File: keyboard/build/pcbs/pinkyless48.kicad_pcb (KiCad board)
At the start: 2 copper layers, 141.4 x 137.9 mm, 51 parts

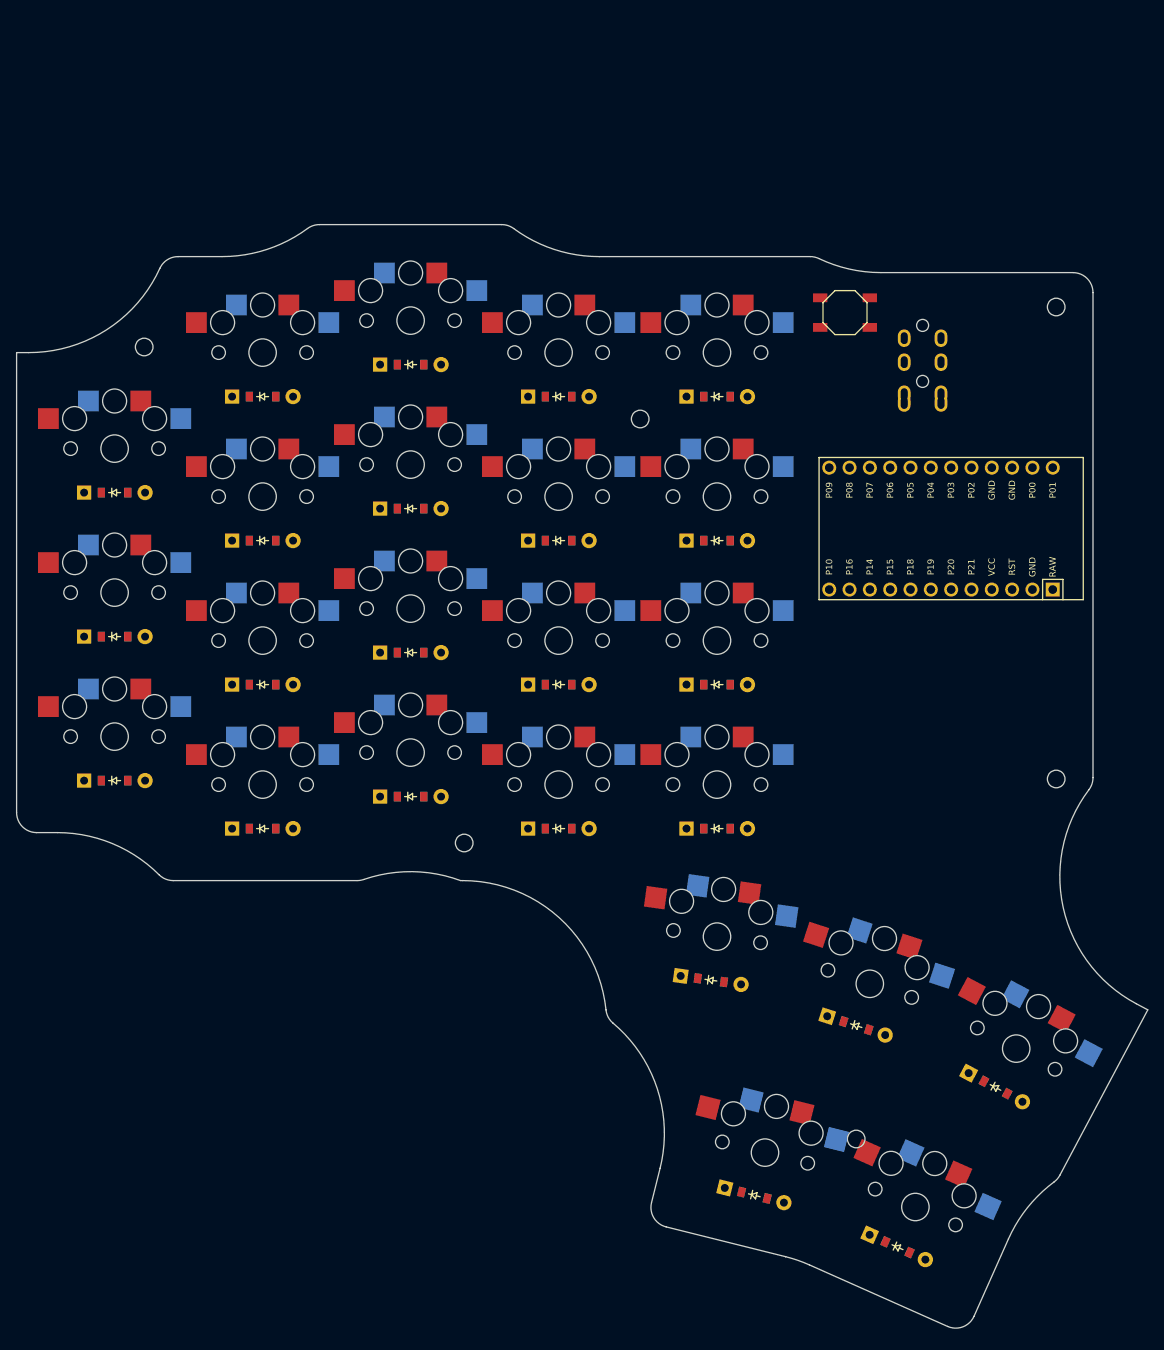
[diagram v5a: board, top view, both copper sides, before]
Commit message: Rebuild the board silhouette from three simple shapes
The outline was the union of one grown rectangle per key, so every column
step and every rotated thumb key left its own scallop and fillet. Straight
runs were constantly interrupted by small arcs, which is exactly what makes a
case hard to build against.

It is now three primitives:

  1. the finger matrix as ONE rectangle spanning every column and row,
     sized parametrically from kx/ky/kx_inner and the staggers
  2. the thumb cluster as a hull over its five keys, with `extend` so the
     hull wraps the key pads rather than the key centres
  3. the controller area as a rectangle

Measured: the fabricated outline goes from a scalloped perimeter to 9 straight
lines + 12 arcs + 6 screw holes, for about 1 cm^2 more copper and a slightly
smaller bounding box (136.4 x 134.1 mm, was 141.4 x 137.9).

This also makes two earlier workarounds redundant, both now removed: the `web`
patch zone that plugged a gap between unioned thumb pads, and the bridges
before it. A single rectangle cannot be disconnected from itself and a hull is
convex, so there is nothing left to bridge.

Fixed a mirroring bug found while rebuilding the preview's right half: an
anchor `shift` on a mirror_ ref has its x auto-negated by ergogen, so the
right half needs the SAME expression as the left, not its negation. Negating
it manually double-flipped the matrix rectangle and put it 75 mm off. Note
that this is the opposite of `adjust` shifts, which are NOT mirrored - the two
behave differently and are easy to get backwards. Both are now commented.

All five checks pass. Case STLs, QMK keyboard.json and previews regenerated.

Co-Authored-By: Claude Opus 5 <noreply@anthropic.com>
Claude-Session: https://claude.ai/code/session_01TKXtddA7pBLooPYbDwxvxo
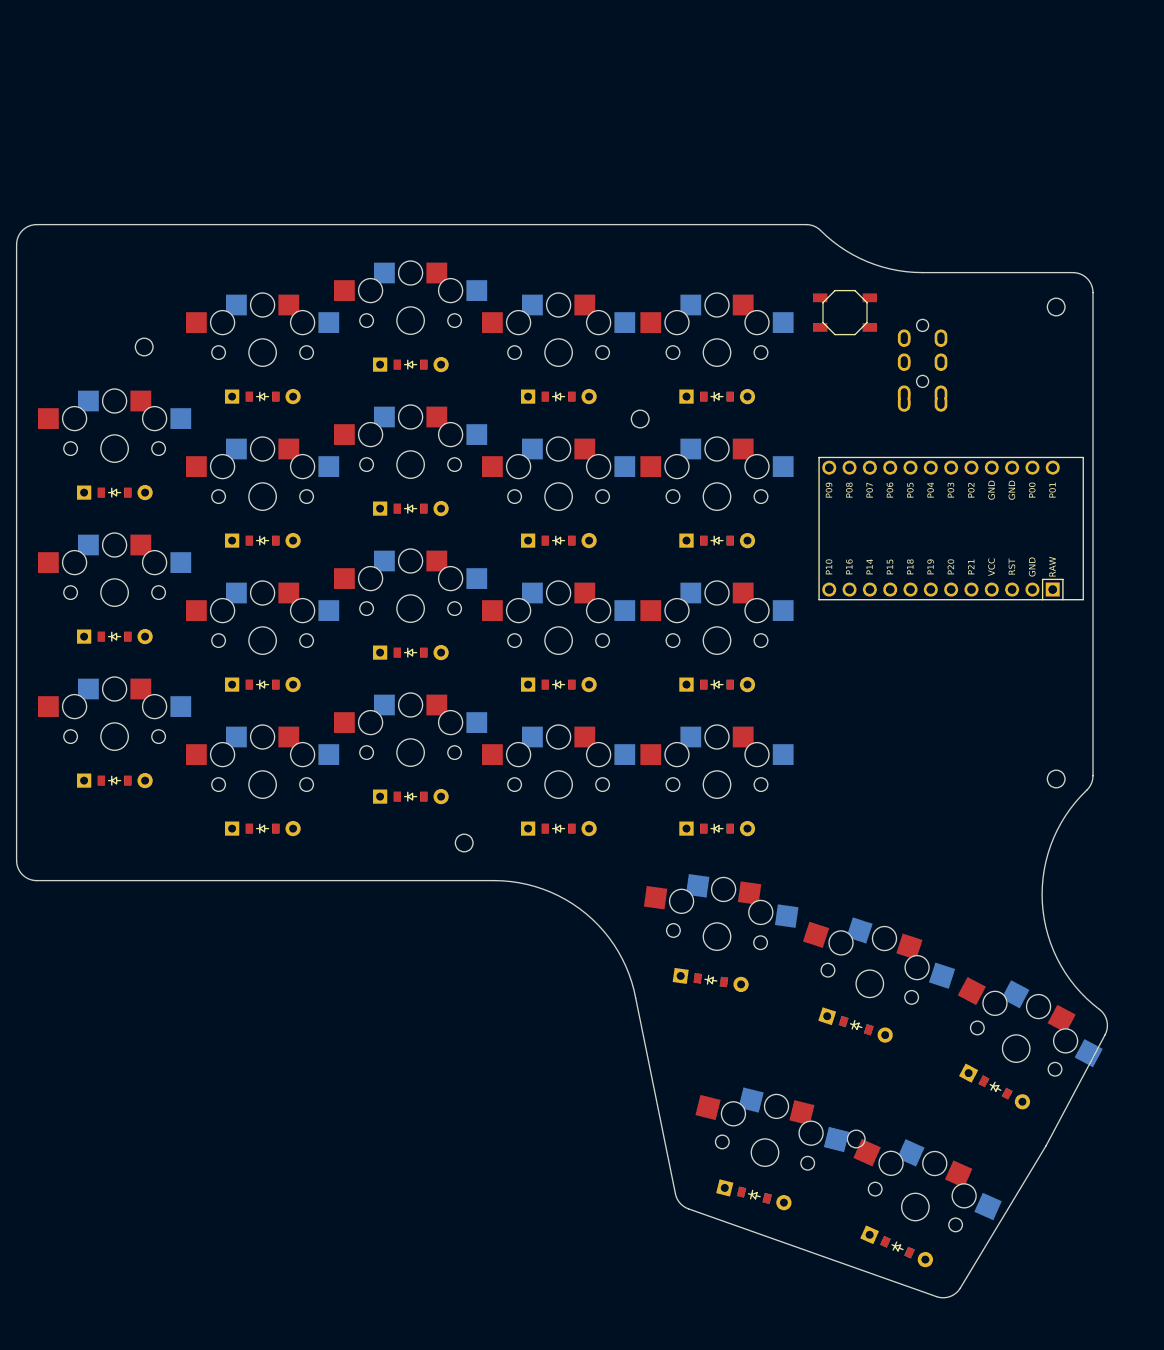
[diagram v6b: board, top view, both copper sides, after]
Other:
- board size 141.4 x 137.9 mm -> 136.4 x 134.1 mm
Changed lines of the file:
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@@
         (pad 2 smd rect (at 3.1 1.85 0) (size 1.8 1.1) (layers F.Cu F.Paste F.Mask) (net 36 "GND"))
     )
-  (gr_line (start 50.25 166) (end 52.833592100000004 166) (angle 90) (layer Edge.Cuts) (width 0.15))
-(gr_arc (start 52.833592100000004 184) (end 65.55772780000001 171.2682927) (angle -44.98295773650154) (layer Edge.Cuts) (width 0.15))
-(gr_line (start 67.32496880000001 172) (end 90.3170334 172) (angle 90) (layer Edge.Cuts) (width 0.15))
-(gr_arc (start 97 188.8800918) (end 103.25 172) (angle -39.343579589725564) (layer Edge.Cuts) (width 0.15))
-(gr_line (start 103.25 172) (end 103.5179019 172) (angle 90) (layer Edge.Cuts) (width 0.15))
-(gr_arc (start 103.5179019 190) (end 121.4232685 188.1566752) (angle -84.12221075760122) (layer Edge.Cuts) (width 0.15))
-(gr_arc (start 110.72322720000001 203.59638109999997) (end 128.1885503 207.95097529999998) (angle -63.96441148293706) (layer Edge.Cuts) (width 0.15))
-(gr_line (start 128.1885503 207.95097529999998) (end 127.11561936668006 212.25426619386195) (angle 90) (layer Edge.Cuts) (width 0.15))
-(gr_line (start 128.93655389320645 215.28481023800936) (end 143.86603395881048 219.0071477146631) (angle 90) (layer Edge.Cuts) (width 0.15))
-(gr_arc (start 139.5114398 236.4724708) (end 146.8326994 220.0286526) (angle -10.000000169783107) (layer Edge.Cuts) (width 0.15))
-(gr_line (start 146.83269944378011 220.02865256083294) (end 164.12622863217297 227.72822781372136) (angle 90) (layer Edge.Cuts) (width 0.15))
-(gr_line (start 167.42693366205984 226.46120582119784) (end 171.73221373092065 216.7913887305511) (angle 90) (layer Edge.Cuts) (width 0.15))
-(gr_arc (start 188.17603180000003 224.1126485) (end 177.43961960000004 209.6651763) (angle -29.382692622423704) (layer Edge.Cuts) (width 0.15))
-(gr_line (start 178.1558201633024 208.83226198048754) (end 189.1497668 188.1556555) (angle 90) (layer Edge.Cuts) (width 0.15))
-(gr_line (start 189.14976710000002 188.1556557) (end 187.7026001 187.3861834) (angle 90) (layer Edge.Cuts) (width 0.15))
-(gr_arc (start 196.1530879 171.49312650000002) (end 181.79427900000002 160.6384221) (angle -99.08787226730266) (layer Edge.Cuts) (width 0.15))
-(gr_line (start 182.3 159.13082430000003) (end 182.3 98.5) (angle 90) (layer Edge.Cuts) (width 0.15))
-(gr_line (start 179.8 96) (end 155.7962113 96) (angle 90) (layer Edge.Cuts) (width 0.15))
-(gr_arc (start 155.7962113 78) (end 148.0414944 94.2439024) (angle -25.519458575786103) (layer Edge.Cuts) (width 0.15))
-(gr_line (start 120.5637085 94) (end 146.9644504 94) (angle 90) (layer Edge.Cuts) (width 0.15))
-(gr_arc (start 120.5637085 76) (end 109.88178400000001 90.4878049) (angle -36.40152061770755) (layer Edge.Cuts) (width 0.15))
-(gr_line (start 108.39818340000001 90) (end 85.60181659999999 90) (angle 90) (layer Edge.Cuts) (width 0.15))
-(gr_arc (start 73.4362915 76) (end 73.4362915 94) (angle -36.40152061770755) (layer Edge.Cuts) (width 0.15))
-(gr_line (start 73.4362915 94) (end 67.9341953 94) (angle 90) (layer Edge.Cuts) (width 0.15))
-(gr_arc (start 49.279437200000004 88) (end 49.279437200000004 106) (angle -65.50372094166266) (layer Edge.Cuts) (width 0.15))
-(gr_line (start 49.279437200000004 106) (end 47.75000000000001 106) (angle 90) (layer Edge.Cuts) (width 0.15))
-(gr_line (start 47.75 163.5) (end 47.75 106) (angle 90) (layer Edge.Cuts) (width 0.15))
-(gr_arc (start 67.32496880000001 169.5) (end 65.5577277 171.2682927) (angle -44.98295773650153) (layer Edge.Cuts) (width 0.15))
-(gr_arc (start 90.3170334 169.5) (end 90.3170334 172) (angle -19.026071927930843) (layer Edge.Cuts) (width 0.15))
-(gr_arc (start 123.910125 187.9006579) (end 121.42326849999999 188.1566752) (angle -44.086622016723254) (layer Edge.Cuts) (width 0.15))
-(gr_arc (start 129.54135865201698 212.85907095267237) (end 127.11561935201698 212.25426615267236) (angle -89.99999999999787) (layer Edge.Cuts) (width 0.15))
-(gr_arc (start 143.2612292 221.432887) (end 143.866034 219.0071477) (angle -5.817540369434937e-7) (layer Edge.Cuts) (width 0.15))
-(gr_arc (start 165.14307009298054 225.4443641517489) (end 164.12622859298054 227.72822785174893) (angle -89.99999476576903) (layer Edge.Cuts) (width 0.15))
-(gr_arc (start 174.01607730000003 217.8082304) (end 171.73221370000005 216.79138870000003) (angle -0.0000014050642107577005) (layer Edge.Cuts) (width 0.15))
-(gr_arc (start 175.94845120000002 207.65858300000002) (end 177.43961960000001 209.6651764) (angle -25.382691519248112) (layer Edge.Cuts) (width 0.15))
-(gr_arc (start 179.8 159.13082430000003) (end 181.79427900000002 160.63842210000004) (angle -37.08787093733031) (layer Edge.Cuts) (width 0.15))
+  (gr_line (start 50.25000000000001 172) (end 107.44764900625802 172) (angle 90) (layer Edge.Cuts) (width 0.15))
+(gr_arc (start 107.44764900625802 190) (end 125.13502950625802 186.6598547) (angle -79.30600510183717) (layer Edge.Cuts) (width 0.15))
+(gr_line (start 125.13502950000003 186.6598547) (end 130.10850241918928 211.16800409522773) (angle 90) (layer Edge.Cuts) (width 0.15))
+(gr_line (start 131.72459050284087 213.02760626035715) (end 162.73886519901427 224.0022760177633) (angle 90) (layer Edge.Cuts) (width 0.15))
+(gr_line (start 165.7139734522696 222.93603710847464) (end 176.38659681858962 205.2293216400106) (angle 90) (layer Edge.Cuts) (width 0.15))
+(gr_line (start 176.4528302479985 205.11244310040672) (end 183.8100726729523 191.27548248561845) (angle 90) (layer Edge.Cuts) (width 0.15))
+(gr_arc (start 193.94004180000002 173.72987360000002) (end 181.5243954 160.69715620000002) (angle -99.38857838211368) (layer Edge.Cuts) (width 0.15))
+(gr_line (start 182.3 158.88705650000003) (end 182.3 98.5) (angle 90) (layer Edge.Cuts) (width 0.15))
+(gr_line (start 179.8 96) (end 160.9664079 96) (angle 90) (layer Edge.Cuts) (width 0.15))
+(gr_arc (start 160.9664079 78) (end 148.2422722 90.7317073) (angle -44.982957736501504) (layer Edge.Cuts) (width 0.15))
+(gr_line (start 146.47503120000002 90) (end 50.25000000000001 90) (angle 90) (layer Edge.Cuts) (width 0.15))
+(gr_line (start 47.75000000000001 92.5) (end 47.75000000000001 169.5) (angle 90) (layer Edge.Cuts) (width 0.15))
+(gr_arc (start 132.55856322695692 210.6708098335049) (end 130.10850242695693 211.1680041335049) (angle -59.04189795921596) (layer Edge.Cuts) (width 0.15))
+(gr_arc (start 163.57283792313032 221.6454795909111) (end 162.73886522313032 224.0022759909111) (angle -78.4075267962939) (layer Edge.Cuts) (width 0.15))
+(gr_arc (start 174.24546128945036 203.93876412244708) (end 176.38659678945035 205.2293216224471) (angle -3.079235708651538) (layer Edge.Cuts) (width 0.15))
+(gr_arc (start 181.6027037 190.10180350000002) (end 183.8100726 191.2754825) (angle -80.99954630283008) (layer Edge.Cuts) (width 0.15))
+(gr_arc (start 179.8 158.88705650000003) (end 181.5243953 160.69715610000003) (angle -46.38903376982785) (layer Edge.Cuts) (width 0.15))
 (gr_arc (start 179.8 98.5) (end 182.3 98.5) (angle -90) (layer Edge.Cuts) (width 0.15))
-(gr_arc (start 146.9644504 96.5) (end 148.0414944 94.2439024) (angle -25.519458575786103) (layer Edge.Cuts) (width 0.15))
-(gr_arc (start 108.39818340000001 92.5) (end 109.88178400000001 90.4878049) (angle -36.40152061770755) (layer Edge.Cuts) (width 0.15))
-(gr_arc (start 85.60181659999999 92.5) (end 85.60181659999999 90) (angle -36.40152061770755) (layer Edge.Cuts) (width 0.15))
-(gr_arc (start 67.9341953 96.5) (end 67.9341953 94) (angle -65.50372094166269) (layer Edge.Cuts) (width 0.15))
-(gr_arc (start 50.25 163.5) (end 47.75 163.5) (angle -90) (layer Edge.Cuts) (width 0.15))
+(gr_arc (start 146.47503120000002 92.5) (end 148.24227230000002 90.7317073) (angle -44.9829577365015) (layer Edge.Cuts) (width 0.15))
+(gr_arc (start 50.25000000000001 92.5) (end 50.25000000000001 90) (angle -90) (layer Edge.Cuts) (width 0.15))
+(gr_arc (start 50.25000000000001 169.5) (end 47.75000000000001 169.5) (angle -90) (layer Edge.Cuts) (width 0.15))
 (gr_circle (center 177.7 100.3) (end 178.79999999999998 100.3) (layer Edge.Cuts) (width 0.15))
 (gr_circle (center 63.7 105.3) (end 64.8 105.3) (layer Edge.Cuts) (width 0.15))
